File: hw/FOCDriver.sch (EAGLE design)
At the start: 106 parts, among them U1 IX4428N, U2 IX4428N, U3 IX4428N, U4 IRF9389TRPBF, U5 IRF9389TRPBF, U6 IRF9389TRPBF, U7 LM27313XMF, U8 MCP6024T-I, U9 TLV3201AIDBVR

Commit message: layout
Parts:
- removed C26: 0.1uF, resistor:C-EUC0805
- removed C28: 56pF, resistor:C-EUC0805
- removed C29: 1nF, resistor:C-EUC0805
- removed FAULT, POWER, PWM1H1, PWM1H2, PWM1H3, PWM1L1, PWM1L2, PWM1L3: (no value), led:LEDSML0805
- removed R47: 30K 1%, resistor:R-EU_R0805
- removed R48: 10K 1%, resistor:R-EU_R0805
- removed R49: 1M 1%, resistor:R-EU_R0805
- removed R50: 13.2K, resistor:R-EU_R0805
- removed R51: 10K, resistor:R-EU_R0805
- removed R52: 300R 1%, resistor:R-EU_R0805
- removed R53: 1K, resistor:R-EU_R0805
- removed SV1: (no value), con-lsta:FE06-1
- removed SV2: (no value), con-lsta:FE08-1
- added J1: (no value), SparkFun-Connectors:CONN_06SILK_FEMALE_PTH
- added J2: (no value), SparkFun-Connectors:CONN_08"
- added LED1, LED2, LED3, LED4, LED5, LED6, LED7: (no value), led:LEDSML0805
- C13: value 4.7uF -> 1nF
- C14: value 0.1uF -> 4.7uF
- C15: value 470uF -> 0.1uF; device resistor:CPOL-USE2.5-6 -> resistor:C-EUC0805
- C16: value 0.1uF -> 470uF; device resistor:C-EUC0805 -> resistor:CPOL-USE2.5-6
- C21, C22: value 1nF -> 0.1uF
- C24: value 0.1uF -> 1nF
- C25: value 33pF -> 1nF
- R14: value 1R -> 1K
- R15: value 0R -> 1R
- R16: value 1K -> 0R
- R21: value 10K -> 1K 1%; device pot:TRIM_EU-CT6 -> resistor:R-EU_R0805
- R22: value 100R -> 1K 1%
- R29: value 2.2K -> 1K 1%
- R33, R34, R35: value 1K 1% -> 30K 1%
- R39, R40, R41: value 30K 1% -> 1K 1%
- R42, R43: value 1K 1% -> 51K
- R44: value 1K 1% -> 3.3K
- R45: value 1K 1% -> 100K; device resistor:R-EU_R0805 -> pot:TRIM_EU-CT6
- R46: value 1.5K 1% -> 1K
- U8: value MCP6024T-I -> LM358N; device MCP6024T-I:MCP6024T-I -> Fairchild-LM358N:LM358N
- U9: value TLV3201AIDBVR -> LM358N; device TLV3201AIDBVR:TLV3201AIDBVR -> Fairchild-LM358N:LM358N
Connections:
- removed net +3V3: C7.1, R14.1, R21.E, R29.2, SV2.2
- removed net FAULT_MC: C28.1, R52.2, R53.2, SV1.4
- removed net N$27: C25.2, R45.2, U9.VIN-
- removed net N$28: R46.1, R47.1, R49.1, U9.VIN+
- removed net N$30: R48.1, R49.2, R52.1, U9.VOUT
- removed net N$44: FAULT.A, R53.1
- new net +5V: C7.1, J2.2, R15.1, R44.2, R45.E
- net +12V: now also C15.1, C16.+, C17.1; no longer C15.+, C16.1, C29.1
- net AGND: now also C15.2, C16.-, C17.2, C24.2, C25.2, R16.2, R25.1, R43.1, U8G$3.GND, U9G$3.GND, X1-2.KL; no longer C15.-, C16.2, C24.1, C25.1, C26.1, C27.2, C28.2, C29.2, FAULT.C, R15.2, R27.1, R47.2, R51.1, U8G5.GND, U9.VSS, X1-1.KL
- net AVDD: now also C21.1, C22.1, R15.2, R42.2, U8G$3.VCC, U9G$3.VCC; no longer C24.2, C26.2, R14.2, R46.2, R48.2, R50.2, U8G5.VCC, U9.VDD
- net GND: now also C27.2, J1.6, J2.1, LED7.C, R16.1, R46.1; no longer C17.2, POWER.C, R15.1, R22.1, SV1.6, SV2.1
- net IMOTORA: now also C23.1, J1.3, R39.2; no longer C21.1, R42.2, SV1.3
- net IMOTORB: now also C24.1, J1.2, R40.2; no longer C22.1, R43.2, SV1.2
- net IMOTORBUS: now also C25.1, J1.1, R41.2; no longer C23.1, R44.2, R45.1, SV1.1
- net N$1: now also X1-1.KL; no longer X1-2.KL
- net N$11: now also R21.2, R27.1; no longer R23.2, R30.1
- net N$12: now also R22.2, R28.1; no longer R24.2, R31.1
- net N$13: now also R27.2, R33.1, U8G$2.-IN; no longer R30.2, R36.1, U8G1.-IN
- net N$14: now also R23.2, R29.1; no longer R25.2, R32.1
- net N$15: now also R28.2, R36.1, U8G$2.+IN; no longer R31.2, R37.1, U8G1.+IN
- net N$16: now also R33.2, R39.1, U8G$2.OUT; no longer R36.2, R42.1, U8G1.OUT
- net N$17: now also R24.2, R30.1; no longer R26.2, R33.1
- net N$18: now also R42.1, R43.2, U9G$2.+IN; no longer C27.1, R50.1, R51.2, U8G4.+IN
- net N$19: now also R29.2, R34.2, U8G$1.-IN; no longer R32.2, R38.2, U8G3.-IN
- net N$20: now also R30.2, R37.1, U8G$1.+IN; no longer R33.2, R39.1, U8G3.+IN
- net N$21: now also R34.1, R40.1, U8G$1.OUT; no longer R38.1, R43.1, U8G3.OUT
- net N$22: now also R25.2, R31.1; no longer R27.2, R34.1
- net N$23: now also R26.2, R32.1; no longer R28.2, R35.1
- net N$24: now also R31.2, R35.2, U9G$1.-IN; no longer R34.2, R40.2, U8G2.-IN
- net N$25: now also R32.2, R38.1, U9G$1.+IN; no longer R35.2, R41.1, U8G2.+IN
- net N$26: now also R35.1, R41.1, U9G$1.OUT; no longer R40.1, R44.1, U8G2.OUT
- net N$29: now also C27.1, R45.A, R46.2; no longer C17.1, R21.A, R22.2
- net N$31: now also LED7.A, R44.1; no longer POWER.A, R29.1
- net N$32: now also LED1.C, LED2.C, LED3.C, LED4.C, LED5.C, LED6.C; no longer PWM1H1.C, PWM1H2.C, PWM1H3.C, PWM1L1.C, PWM1L2.C, PWM1L3.C
- net N$33: now also LED1.A; no longer PWM1H1.A
- net N$34: now also LED2.A; no longer PWM1L1.A
- net N$35: now also LED3.A; no longer PWM1H2.A
- net N$36: now also LED4.A, R14.1; no longer PWM1L2.A, R16.1
- net N$37: now also LED5.A; no longer PWM1H3.A
- net N$38: now also LED6.A; no longer PWM1L3.A
- net POT: now also J1.5, R45.S; no longer R21.S, SV1.5
- net PWM1H1: now also J2.3; no longer SV2.3
- net PWM1H2: now also J2.5; no longer SV2.5
- net PWM1H3: now also J2.7; no longer SV2.7
- net PWM1L1: now also J2.4; no longer SV2.4
- net PWM1L2: now also J2.6, R14.2; no longer R16.2, SV2.6
- net PWM1L3: now also J2.8; no longer SV2.8
- net SHUNT_COM: now also R21.1, R26.1; no longer R25.1, R28.1
- net SHUNT_IU: now also R22.1; no longer R24.1
- net SHUNT_IV: now also R24.1; no longer R26.1
- net VREF: now also R36.2, R38.2, U9G$2.-IN, U9G$2.OUT; no longer R39.2, R41.2, U8G4.-IN, U8G4.OUT
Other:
- note removed: "V3.3"
- note removed: "VREF=half of AVDD voltage"
- moved on the sheet: C12, C13, C14, C21, C22, C23, C24, C25, C27, R22, R23, R24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

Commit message: layout
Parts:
- removed J1: (no value), SparkFun-Connectors:CONN_06SILK_FEMALE_PTH
- removed JP1: (no value), jumper:JP1E
- added C26, C28, C29, C30: 0.1uF, SparkFun-Capacitors:1.0UF-0805-25V-10%
- added J4: (no value), SparkFun-Connectors:CONN_08"
- C1, C2, C3: value 1uF -> 1.0uF; device resistor:C-EUC0805 -> SparkFun-Capacitors:1.0UF-0805-25V-10%
- C10, C11, C27, C4, C5, C6, C7, C8, C9: device resistor:C-EUC0805 -> SparkFun-Capacitors:1.0UF-0805-25V-10%
- C12, C21, C22: value 0.1uF -> 1nF; device resistor:C-EUC0805 -> SparkFun-Capacitors:1.0UF-0805-25V-10%
- C13: value 1nF -> 4.7uF; device resistor:C-EUC0805 -> SparkFun-Capacitors:1.0UF-0805-25V-10%
- C14: value 4.7uF -> 470uF; device resistor:C-EUC0805 -> resistor:CPOL-USE2.5-6
- C15, C17: value 0.1uF -> 56pF; device resistor:C-EUC0805 -> SparkFun-Capacitors:1.0UF-0805-25V-10%
- C16: value 470uF -> 56pF; device resistor:CPOL-USE2.5-6 -> SparkFun-Capacitors:1.0UF-0805-25V-10%
- C18, C19: value 56pF -> 0.1uF; device resistor:C-EUC0805 -> SparkFun-Capacitors:1.0UF-0805-25V-10%
- C20: value 56pF -> 1nF; device resistor:C-EUC0805 -> SparkFun-Capacitors:1.0UF-0805-25V-10%
- C23, C24, C25: value 1nF -> 0.1uF; device resistor:C-EUC0805 -> SparkFun-Capacitors:1.0UF-0805-25V-10%
- R1, R3: value 4.7K -> 4.7K; device resistor:R-EU_R0805 -> SparkFun-Resistors:RESISTOR0805
- R10: value 1K -> 51K; device resistor:R-EU_R0805 -> SparkFun-Resistors:RESISTOR0805
- R11: value 1K -> 13.3K; device resistor:R-EU_R0805 -> SparkFun-Resistors:RESISTOR0805
- R12: value 1K -> 118K; device resistor:R-EU_R0805 -> SparkFun-Resistors:RESISTOR0805
- R13: value 51K -> 1K 1%; device resistor:R-EU_R0805 -> SparkFun-Resistors:RESISTOR0805
- R14, R17, R18: value 1K -> 1K 1%; device resistor:R-EU_R0805 -> SparkFun-Resistors:RESISTOR0805
- R15: value 1R -> 1K 1%; device resistor:R-EU_R0805 -> SparkFun-Resistors:RESISTOR0805
- R16: value 0R -> 1K 1%; device resistor:R-EU_R0805 -> SparkFun-Resistors:RESISTOR0805
- R19: value 13.3K -> 1K 1%; device resistor:R-EU_R0805 -> SparkFun-Resistors:RESISTOR0805
- R2, R21, R22, R23, R24, R4, R46, R5, R6: device resistor:R-EU_R0805 -> SparkFun-Resistors:RESISTOR0805
- R20: value 118K -> 1K 1%; device resistor:R-EU_R0805 -> SparkFun-Resistors:RESISTOR0805
- R25, R26: value 1K 1% -> 51K; device resistor:R-EU_R0805 -> SparkFun-Resistors:RESISTOR0805
- R27, R28, R29, R30, R31, R32: value 1K 1% -> 30K 1%; device resistor:R-EU_R0805 -> SparkFun-Resistors:RESISTOR0805
- R33, R34, R35: value 30K 1% -> 1K 1%; device resistor:R-EU_R0805 -> SparkFun-Resistors:RESISTOR0805
- R36: value 30K 1% -> 1R; device resistor:R-EU_R0805 -> SparkFun-Resistors:RESISTOR0805
- R37: value 30K 1% -> 0R; device resistor:R-EU_R0805 -> SparkFun-Resistors:RESISTOR0805
- R38: value 30K 1% -> 1K; device resistor:R-EU_R0805 -> SparkFun-Resistors:RESISTOR0805
- R39, R40, R41: value 1K 1% -> 1K; device resistor:R-EU_R0805 -> SparkFun-Resistors:RESISTOR0805
- R42: value 51K -> 1K; device resistor:R-EU_R0805 -> SparkFun-Resistors:RESISTOR0805
- R43: value 51K -> 3.3K; device resistor:R-EU_R0805 -> SparkFun-Resistors:RESISTOR0805
- R44: value 3.3K -> 1K; device resistor:R-EU_R0805 -> SparkFun-Resistors:RESISTOR0805
- R7, R8, R9: device resistor:R-EU_R2512 -> resistor:R-US_R2512
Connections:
- removed net N$32: JP1.2, LED1.C, LED2.C, LED3.C, LED4.C, LED5.C, LED6.C
- removed net N$38 (its old number): LED6.A, R18.1
- new net LEDJP1: J4.6, LED1.C, LED2.C, LED3.C, LED4.C, LED5.C, LED7.C
- new net N$31: LED6.A, R43.1
- net +12V: now also C1.1, C10.1, C14.+, C2.1, C3.1, C4.1, C5.1, C6.1, C7.1, C9.1, R12.2; no longer C1.2, C14.1, C15.1, C16.+, C17.1, C2.2, C3.2, C4.2, C5.2, C6.2, R20.2
- net +5V: now also C23.1, J2.1, R36.1, R43.2; no longer C7.1, J2.2, R15.1, R44.2
- net AGND: now also C1.2, C10.2, C14.-, C18.2, C19.2, C2.2, C20.2, C27.2, C28.2, C29.2, C3.2, C30.2, C4.2, C5.2, C6.2, C7.2, R11.1, R17.1, R26.1, R37.2, R9.2; no longer C1.1, C10.1, C14.2, C15.2, C16.-, C17.2, C2.1, C23.2, C3.1, C4.1, C5.1, C6.1, R16.2, R19.1, R25.1, R43.1, R9.1
- net AVDD: now also C18.1, C19.1, C24.1, C25.1, R25.2, R36.2; no longer C10.2, C21.1, C22.1, C9.1, R15.2, R42.2
- net GND: now also C23.2, C26.2, J2.2, J4.7, J4.8, LED6.C, R37.1; no longer C27.2, C7.2, J1.6, J2.1, JP1.1, LED7.C, R16.1
- net IMOTORA: now also C20.1, J4.3, R33.2; no longer C23.1, J1.3, R39.2
- net IMOTORB: now also C21.1, J4.2, R34.2; no longer C24.1, J1.2, R40.2
- net IMOTORBUS: now also C22.1, J4.1, R35.2; no longer C25.1, J1.1, R41.2
- net N$1: now also R10.1; no longer R13.1
- net N$11: now also C15.1, R13.2, R19.1; no longer C18.2, R21.2, R27.1
- net N$12: now also C15.2, R14.2, R20.1; no longer C18.1, R22.2, R28.1
- net N$13: now also R19.2, R27.1; no longer R27.2, R33.1
- net N$14: now also C16.1, R15.2, R21.1; no longer C19.2, R23.2, R29.1
- net N$15: now also R20.2, R30.1; no longer R28.2, R36.1
- net N$16: now also R27.2, R33.1; no longer R33.2, R39.1
- net N$17: now also C16.2, R16.2, R22.1; no longer C19.1, R24.2, R30.1
- net N$18: now also C27.1, R25.1, R26.2; no longer R42.1, R43.2
- net N$19: now also R21.2, R28.1; no longer R29.2, R34.2
- net N$2: now also R10.2; no longer R13.2
- net N$20: now also R22.2, R31.1; no longer R30.2, R37.1
- net N$21: now also R28.2; no longer R40.1
- net N$22: now also C17.1, R17.2, R23.1; no longer C20.2, R25.2, R31.1
- net N$23: now also C17.2, R18.2, R24.1; no longer C20.1, R26.2, R32.1
- net N$24: now also R23.2, R29.1; no longer R31.2, R35.2
- net N$25: now also R24.2, R32.1; no longer R32.2, R38.1
- net N$26: now also R29.2; no longer R41.1
- net N$29: now also C26.1; no longer C27.1
- net N$33: now also R38.1; no longer R10.1
- net N$34: now also R39.1; no longer R11.1
- net N$35: now also R40.1; no longer R12.1
- net N$36: now also R41.1; no longer R14.1
- net N$37: now also R42.1; no longer R17.1
- net N$4: now also R11.2, R12.1; no longer R19.2, R20.1
- net POT: now also J4.5; no longer J1.5
- net PWM1H1: now also R38.2; no longer R10.2
- net PWM1H2: now also R40.2; no longer R12.2
- net PWM1H3: now also R42.2; no longer R17.2
- net PWM1L1: now also R39.2; no longer R11.2
- net PWM1L2: now also R41.2; no longer R14.2
- net PWM1L3: now also R44.2; no longer R18.2
- net SHUNT_COM: now also R13.1, R15.1, R18.1, R7.2, R8.2, R9.1; no longer R21.1, R23.1, R26.1, R7.1, R8.1, R9.2
- net SHUNT_IU: now also R14.1, R7.1; no longer R22.1, R7.2
- net SHUNT_IV: now also R16.1, R8.1; no longer R24.1, R8.2
- net VREF: now also C28.1, C29.1, C30.1, R30.2, R31.2, R32.2; no longer R36.2, R37.2, R38.2
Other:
- note added: "PWM LED ON/OFF"
- moved on the sheet: C1, C12, C13, C18, C19, C2, C20, C21, C22, C23, C24, C25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

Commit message: layout
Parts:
- removed LED1, LED2, LED3, LED4, LED5, LED7: (no value), led:LEDSML0805
- added PWM1H1, PWM1H2, PWM1H3, PWM1L1, PWM1L2, PWM1L3: (no value), led:LEDSML0805
- C20, C21, C22: value 1nF -> 0.1uF
- C24, C25, C26: value 0.1uF -> 1nF
- R36: value 1R -> 1K
- R37: value 0R -> 1K
- R38: value 1K -> 1R
- R39: value 1K -> 0R
- R43: value 3.3K -> 1K
- R44: value 1K -> 3.3K
- renumbered J4 to J1, LED6 to POWER
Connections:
- net +5V: now also C27.1, R38.1, R44.2; no longer C23.1, R36.1, R43.2
- net AGND: now also C23.2, C26.2, R39.2; no longer C27.2, C30.2, R37.2
- net AVDD: now also C20.1, C28.1, C29.1, R38.2; no longer C18.1, C24.1, C25.1, R36.2
- net GND: now also C27.2, C30.2, R39.1; no longer C23.2, C26.2, R37.1
- net IMOTORA: now also C24.1; no longer C20.1
- net IMOTORB: now also C25.1; no longer C21.1
- net IMOTORBUS: now also C26.1; no longer C22.1
- net LEDJP1: now also PWM1H1.C, PWM1H2.C, PWM1H3.C, PWM1L1.C, PWM1L2.C, PWM1L3.C; no longer LED1.C, LED2.C, LED3.C, LED4.C, LED5.C, LED7.C
- net N$18: now also C18.1; no longer C27.1
- net N$29: now also C30.1; no longer C26.1
- net N$31: now also R44.1; no longer R43.1
- net N$33: now also PWM1H1.A, R36.1; no longer LED1.A, R38.1
- net N$34: now also PWM1L1.A, R37.1; no longer LED2.A, R39.1
- net N$35: now also PWM1H2.A; no longer LED3.A
- net N$36: now also PWM1L2.A; no longer LED4.A
- net N$37: now also PWM1H3.A; no longer LED5.A
- net N$38: now also PWM1L3.A, R43.1; no longer LED7.A, R44.1
- net PWM1H1: now also R36.2; no longer R38.2
- net PWM1L1: now also R37.2; no longer R39.2
- net PWM1L3: now also R43.2; no longer R44.2
- net VREF: now also C21.1, C22.1, C23.1; no longer C28.1, C29.1, C30.1
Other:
- moved on the sheet: C18, C19, C20, C21, C22, C23, C24, C25, C26, C27, C28, C29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

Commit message: packages
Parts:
- added X3: (no value), con-wago-508:W237-02P
- C14: device resistor:CPOL-USE2.5-6 -> rcl:CPOL-USE2.5-7
- R1, R3: value 4.7K -> 4.7K
- R26: value 51K -> 51K
- R33, R34, R35: value 1K 1% -> 1K 1%
- R36, R37, R40, R41, R42, R43: value 1K -> 1K
- R45: value 100K -> (none); device pot:TRIM_EU-CT6 -> pot:TRIM_US-CT6
- X1: device con-wago-500:W237-102 -> con-wago-508:W237-02P
- X2: device con-wago-500:W237-4 -> con-wago-508:W237-02P
- renumbered POWER to LED7, PWM1H1 to LED1, PWM1H2 to LED3, PWM1H3 to LED5, PWM1L1 to LED2, PWM1L2 to LED4, PWM1L3 to LED6
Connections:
- net AGND: now also X1-1.KL; no longer X1-2.KL
- net M1: now also X2-1.KL; no longer X2-2.KL
- net M2: now also X3-2.KL; no longer X2-3.KL
- net M3: now also X3-1.KL; no longer X2-4.KL
- net N$1: now also X1-2.KL; no longer X1-1.KL

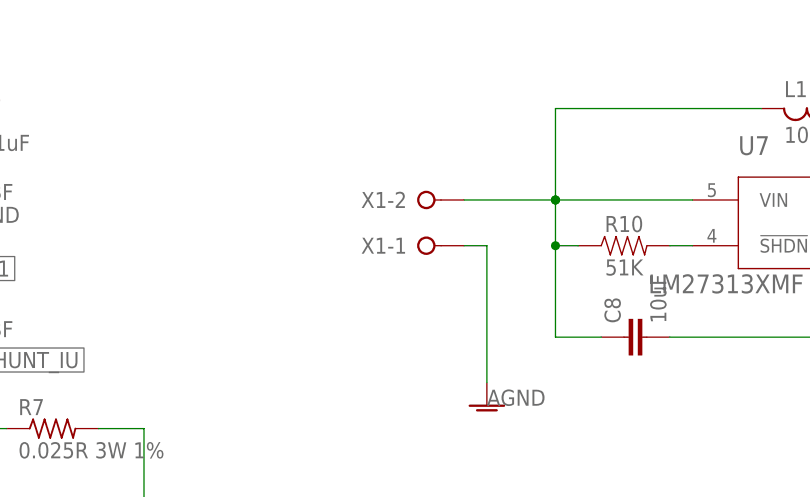
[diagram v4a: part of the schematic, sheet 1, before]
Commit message: add resettable fuse
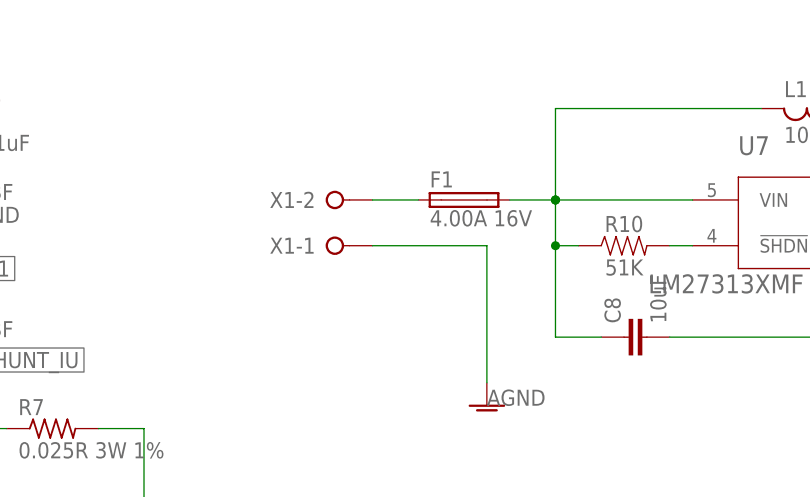
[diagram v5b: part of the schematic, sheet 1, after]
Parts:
- added F1: 4.00A 16V, fuse:TE5
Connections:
- new net N$27: F1.1, X1-2.KL
- net N$1: now also F1.2; no longer X1-2.KL
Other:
- moved on the sheet: X1-1, X1-2
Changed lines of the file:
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@@
 <part name="X1" library="con-wago-508" deviceset="W237-02P" device=""/>
 <part name="R45" library="pot" deviceset="TRIM_US-" device="CT6"/>
+<part name="F1" library="fuse" deviceset="TE5" device="" value="4.00A 16V"/>
 </parts>
 <sheets>
@@
 <instance part="J1" gate="G$1" x="233.68" y="101.6" rot="R180"/>
 <instance part="C14" gate="G$1" x="241.3" y="142.24"/>
-<instance part="X1" gate="-1" x="134.62" y="147.32"/>
-<instance part="X1" gate="-2" x="134.62" y="152.4"/>
+<instance part="X1" gate="-1" x="124.46" y="147.32"/>
+<instance part="X1" gate="-2" x="124.46" y="152.4"/>
+<instance part="F1" gate="1" x="139.7" y="152.4"/>
 </instances>
 <busses>
@@
 <pinref part="X1" gate="-1" pin="KL"/>
 <wire x1="142.24" y1="132.08" x2="142.24" y2="147.32" width="0.1524" layer="91"/>
-<wire x1="142.24" y1="147.32" x2="139.7" y2="147.32" width="0.1524" layer="91"/>
+<wire x1="142.24" y1="147.32" x2="129.54" y2="147.32" width="0.1524" layer="91"/>
 </segment>
 <segment>
@@
 <pinref part="R10" gate="G$1" pin="1"/>
 <pinref part="C8" gate="G$1" pin="1"/>
-<pinref part="X1" gate="-2" pin="KL"/>
-<wire x1="139.7" y1="152.4" x2="149.86" y2="152.4" width="0.1524" layer="91"/>
+<pinref part="F1" gate="1" pin="2"/>
+<wire x1="144.78" y1="152.4" x2="149.86" y2="152.4" width="0.1524" layer="91"/>
 </segment>
 </net>
@@
 </segment>
 </net>
+<net name="N$27" class="3">
+<segment>
+<pinref part="X1" gate="-2" pin="KL"/>
+<pinref part="F1" gate="1" pin="1"/>
+<wire x1="134.62" y1="152.4" x2="129.54" y2="152.4" width="0.1524" layer="91"/>
+</segment>
+</net>

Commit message: trans
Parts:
- removed C10: 0.1uF, SparkFun-Capacitors:1.0UF-0805-25V-10%
- removed U1, U2, U3: IX4428N, IX4428N:IX4428N
- added Q1, Q2, Q3, Q4, Q5, Q6: BC546B, transistor-npn:BC546B
- added R47, R50: 330, SparkFun-Resistors:RESISTOR0805
- added R48, R51: 180, SparkFun-Resistors:RESISTOR0805
- added R49: 1K, SparkFun-Resistors:RESISTOR0805
- added R52: 100, SparkFun-Resistors:RESISTOR0805
- C7, C9: value 0.1uF -> 10uF
- R1, R3, R4: value 4.7K -> 1K
- R2: value 4.7K -> 100
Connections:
- new net N$28: Q1.E, R48.1
- new net N$30: Q1.B, R1.2
- new net N$32: Q2.B, R49.2
- new net N$39: Q3.B, R3.2
- new net N$40: Q3.E, R51.1
- new net N$41: Q4.B, R4.2
- net +12V: now also R47.2, R50.2; no longer C10.1, U1C.VCC, U2C.VCC, U3C.VCC
- net AGND: no longer C10.2, C7.2, C9.2, U1C.GND, U2C.GND, U3C.GND
- net GND: now also Q2.E, Q4.E, R48.2, R51.2; no longer R1.1, R2.1, R3.1, R4.1
- net N$10: now also C7.2, Q1.C, R47.1; no longer U1A.O
- net N$3: no longer U3B.O
- net N$6: no longer U3A.O
- net N$7: now also Q4.C, R52.2; no longer U2B.O
- net N$8: now also C9.2, Q3.C, R50.1; no longer U2A.O
- net N$9: now also Q2.C, R2.2; no longer U1B.O
- net PWM1H1: now also R1.1, R49.1; no longer R1.2, U1A.I
- net PWM1H2: now also R3.1, R4.1; no longer R3.2, U2A.I
- net PWM1H3: no longer U3A.I
- net PWM1L1: now also R2.1; no longer R2.2, U1B.I
- net PWM1L2: now also R52.1; no longer R4.2, U2B.I
- net PWM1L3: no longer U3B.I
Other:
- moved on the sheet: C7, C9, R1, R2, R3, R4
